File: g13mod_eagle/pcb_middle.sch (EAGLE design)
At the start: 14 parts

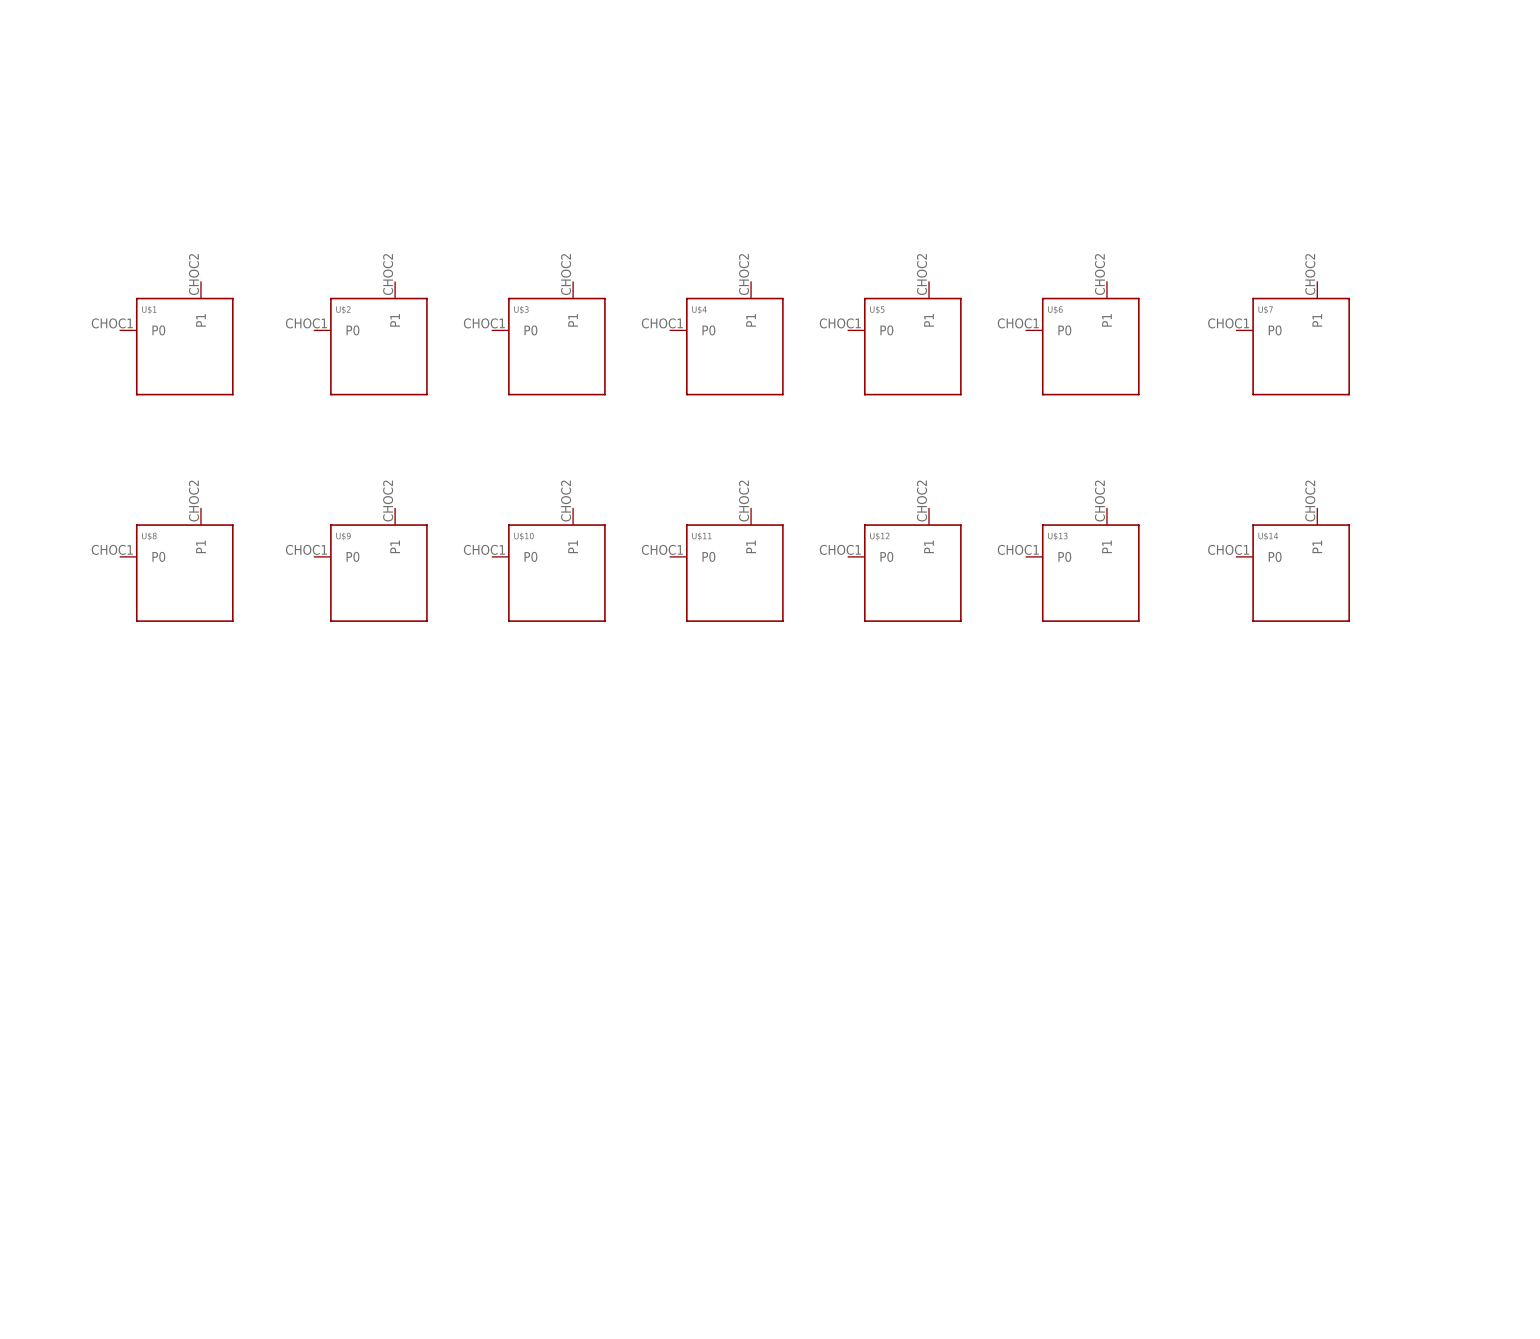
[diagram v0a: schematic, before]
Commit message: wiring middle pcb
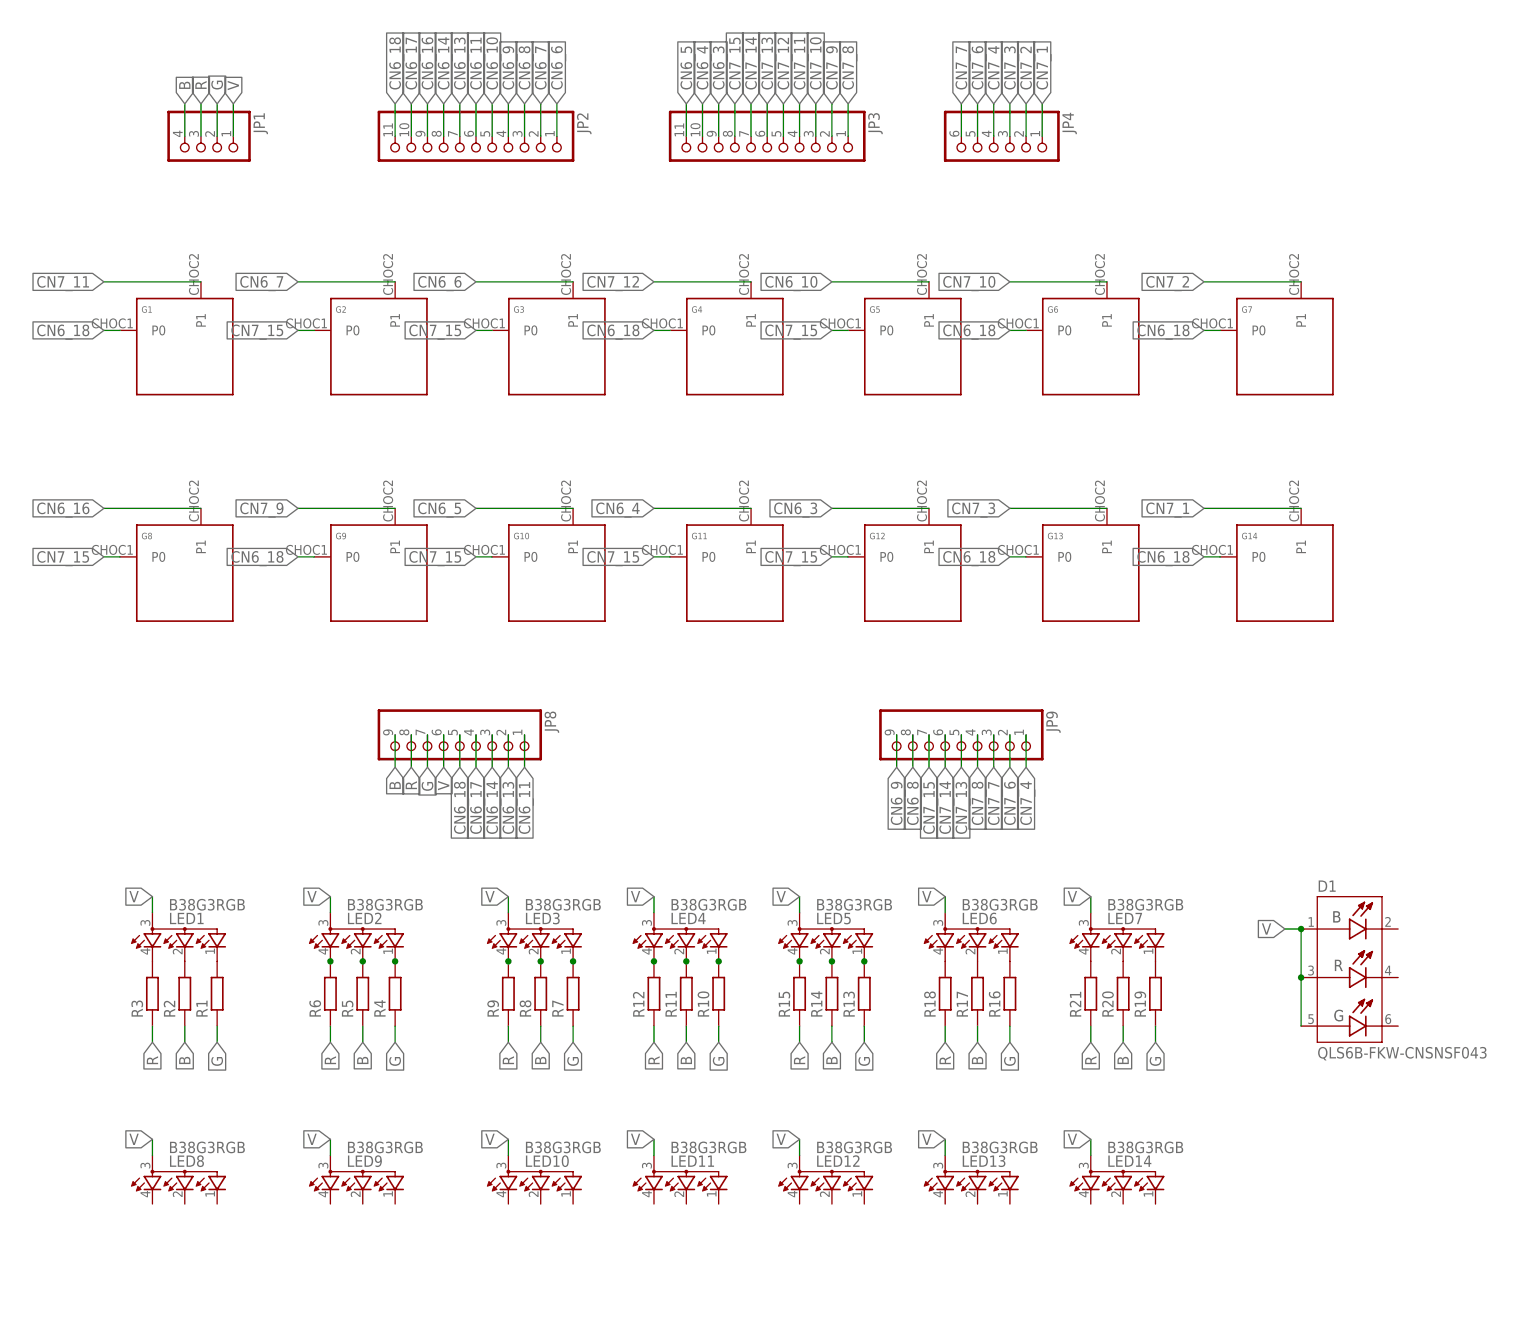
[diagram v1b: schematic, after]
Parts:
- removed U$14, U$7: KEYSWITCH-PLAIN-CHOC-1U, Keyboard:KEYSWITCH-PLAIN-CHOC-1U
- added D1: QLS6B-FKW-CNSNSF043, QLS6B-FKW-CNSNSF043:QLS6B-FKW-CNSNSF043
- added G14, G7: KEYSWITCH-PLAIN-CHOC-1U, Keyboard:KEYSWITCH-PLAIN-CHOC-1U
- added JP1: (no value), pinhead-half-pitch:THROUHOLE04
- added JP2, JP3: (no value), pinhead-half-pitch:THROUHOLE11
- added JP4: (no value), pinhead-half-pitch:THROUHOLE06
- added JP8, JP9: (no value), pinhead-half-pitch:THROUHOLE09
- added LED1, LED10, LED11, LED12, LED13, LED14, LED2, LED3, LED4, LED5, LED6, LED7, LED8, LED9: B38G3RGB, led_rgb:B38G3RGB
- added R1, R10, R11, R12, R13, R14, R15, R16, R17, R18, R19, R2, R20, R21, R3, R4, R5, R6, R7, R8, R9: (no value), rcl:R-EU_R0603
- renumbered U$1 to G1, U$10 to G10, U$11 to G11, U$12 to G12, U$13 to G13, U$2 to G2, U$3 to G3, U$4 to G4, U$5 to G5, U$6 to G6, U$8 to G8, U$9 to G9
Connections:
- new net B: JP1.4, JP8.9, R11.1, R14.1, R17.1, R2.1, R20.1, R5.1, R8.1
- new net CN6_10: G5.P1, JP2.5
- new net CN6_11: JP2.6, JP8.1
- new net CN6_13: JP2.7, JP8.2
- new net CN6_14: JP2.8, JP8.3
- new net CN6_16: G8.P1, JP2.9
- new net CN6_17: JP2.10, JP8.4
- new net CN6_18: G1.P0, G13.P0, G14.P0, G4.P0, G6.P0, G7.P0, G9.P0, JP2.11, JP8.5
- new net CN6_3: G12.P1, JP3.9
- new net CN6_4: G11.P1, JP3.10
- new net CN6_5: G10.P1, JP3.11
- new net CN6_6: G3.P1, JP2.1
- new net CN6_7: G2.P1, JP2.2
- new net CN6_8: JP2.3, JP9.8
- new net CN6_9: JP2.4, JP9.9
- new net CN7_1: G14.P1, JP4.1
- new net CN7_10: G6.P1, JP3.3
- new net CN7_11: G1.P1, JP3.4
- new net CN7_12: G4.P1, JP3.5
- new net CN7_13: JP3.6, JP9.5
- new net CN7_14: JP3.7, JP9.6
- new net CN7_15: G10.P0, G11.P0, G12.P0, G2.P0, G3.P0, G5.P0, G8.P0, JP3.8, JP9.7
- new net CN7_2: G7.P1, JP4.2
- new net CN7_3: G13.P1, JP4.3
- new net CN7_4: JP4.4, JP9.1
- new net CN7_6: JP4.5, JP9.2
- new net CN7_7: JP4.6, JP9.3
- new net CN7_8: JP3.1, JP9.4
- new net CN7_9: G9.P1, JP3.2
- new net G: JP1.2, JP8.7, R1.1, R10.1, R13.1, R16.1, R19.1, R4.1, R7.1
- new net N$1: LED1.CGREEN, R1.2
- new net N$10: LED4.CGREEN, R10.2
- new net N$11: LED4.CBLUE, R11.2
- new net N$12: LED4.CRED, R12.2
- new net N$13: LED5.CGREEN, R13.2
- new net N$14: LED5.CBLUE, R14.2
- new net N$15: LED5.CRED, R15.2
- new net N$16: LED6.CGREEN, R16.2
- new net N$17: LED6.CBLUE, R17.2
- new net N$18: LED6.CRED, R18.2
- new net N$19: LED7.CGREEN, R19.2
- new net N$2: LED1.CBLUE, R2.2
- new net N$20: LED7.CBLUE, R20.2
- new net N$21: LED7.CRED, R21.2
- new net N$3: LED1.CRED, R3.2
- new net N$4: LED2.CGREEN, R4.2
- new net N$5: LED2.CBLUE, R5.2
- new net N$6: LED2.CRED, R6.2
- new net N$7: LED3.CGREEN, R7.2
- new net N$8: LED3.CBLUE, R8.2
- new net N$9: LED3.CRED, R9.2
- new net R: JP1.3, JP8.8, R12.1, R15.1, R18.1, R21.1, R3.1, R6.1, R9.1
- new net V: D1.BLUE_ANODE, D1.GREEN_ANODE, D1.RED_ANODE, JP1.1, JP8.6, LED1.A, LED10.A, LED11.A, LED12.A, LED13.A, LED14.A, LED2.A, LED3.A, LED4.A, LED5.A, LED6.A, LED7.A, LED8.A, LED9.A

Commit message: wiring middle pcb
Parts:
- added R22, R23, R24, R25, R26, R27, R28, R29, R30: (no value), rcl:R-EU_R0603
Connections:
- new net N$22: LED8.CGREEN, R22.2
- new net N$23: LED8.CBLUE, R23.2
- new net N$24: LED8.CRED, R24.2
- new net N$25: LED9.CGREEN, R25.2
- new net N$26: LED9.CBLUE, R26.2
- new net N$27: LED9.CRED, R27.2
- new net N$28: LED10.CGREEN, R28.2
- new net N$29: LED10.CBLUE, R29.2
- new net N$30: LED10.CRED, R30.2
- net B: now also R23.1, R26.1, R29.1
- net G: now also R22.1, R25.1, R28.1
- net R: now also R24.1, R27.1, R30.1
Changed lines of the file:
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@@
 <part name="R20" library="rcl" library_urn="urn:adsk.eagle:library:334" deviceset="R-EU_" device="R0603" package3d_urn="urn:adsk.eagle:package:23555/3"/>
 <part name="R21" library="rcl" library_urn="urn:adsk.eagle:library:334" deviceset="R-EU_" device="R0603" package3d_urn="urn:adsk.eagle:package:23555/3"/>
+<part name="R22" library="rcl" library_urn="urn:adsk.eagle:library:334" deviceset="R-EU_" device="R0603" package3d_urn="urn:adsk.eagle:package:23555/3"/>
+<part name="R23" library="rcl" library_urn="urn:adsk.eagle:library:334" deviceset="R-EU_" device="R0603" package3d_urn="urn:adsk.eagle:package:23555/3"/>
+<part name="R24" library="rcl" library_urn="urn:adsk.eagle:library:334" deviceset="R-EU_" device="R0603" package3d_urn="urn:adsk.eagle:package:23555/3"/>
+<part name="R25" library="rcl" library_urn="urn:adsk.eagle:library:334" deviceset="R-EU_" device="R0603" package3d_urn="urn:adsk.eagle:package:23555/3"/>
+<part name="R26" library="rcl" library_urn="urn:adsk.eagle:library:334" deviceset="R-EU_" device="R0603" package3d_urn="urn:adsk.eagle:package:23555/3"/>
+<part name="R27" library="rcl" library_urn="urn:adsk.eagle:library:334" deviceset="R-EU_" device="R0603" package3d_urn="urn:adsk.eagle:package:23555/3"/>
+<part name="R28" library="rcl" library_urn="urn:adsk.eagle:library:334" deviceset="R-EU_" device="R0603" package3d_urn="urn:adsk.eagle:package:23555/3"/>
+<part name="R29" library="rcl" library_urn="urn:adsk.eagle:library:334" deviceset="R-EU_" device="R0603" package3d_urn="urn:adsk.eagle:package:23555/3"/>
+<part name="R30" library="rcl" library_urn="urn:adsk.eagle:library:334" deviceset="R-EU_" device="R0603" package3d_urn="urn:adsk.eagle:package:23555/3"/>
 </parts>
 <sheets>
@@
 <attribute name="VALUE" x="158.242" y="-87.63" size="1.778" layer="96" rot="R90"/>
 </instance>
+<instance part="R22" gate="G$1" x="17.78" y="-121.92" smashed="yes" rot="R90">
+<attribute name="NAME" x="16.2814" y="-125.73" size="1.778" layer="95" rot="R90"/>
+<attribute name="VALUE" x="21.082" y="-125.73" size="1.778" layer="96" rot="R90"/>
+</instance>
+<instance part="R23" gate="G$1" x="12.7" y="-121.92" smashed="yes" rot="R90">
+<attribute name="NAME" x="11.2014" y="-125.73" size="1.778" layer="95" rot="R90"/>
+<attribute name="VALUE" x="16.002" y="-125.73" size="1.778" layer="96" rot="R90"/>
+</instance>
+<instance part="R24" gate="G$1" x="7.62" y="-121.92" smashed="yes" rot="R90">
+<attribute name="NAME" x="6.1214" y="-125.73" size="1.778" layer="95" rot="R90"/>
+<attribute name="VALUE" x="10.922" y="-125.73" size="1.778" layer="96" rot="R90"/>
+</instance>
+<instance part="R25" gate="G$1" x="45.72" y="-121.92" smashed="yes" rot="R90">
+<attribute name="NAME" x="44.2214" y="-125.73" size="1.778" layer="95" rot="R90"/>
+<attribute name="VALUE" x="49.022" y="-125.73" size="1.778" layer="96" rot="R90"/>
+</instance>
+<instance part="R26" gate="G$1" x="40.64" y="-121.92" smashed="yes" rot="R90">
+<attribute name="NAME" x="39.1414" y="-125.73" size="1.778" layer="95" rot="R90"/>
+<attribute name="VALUE" x="43.942" y="-125.73" size="1.778" layer="96" rot="R90"/>
+</instance>
+<instance part="R27" gate="G$1" x="35.56" y="-121.92" smashed="yes" rot="R90">
+<attribute name="NAME" x="34.0614" y="-125.73" size="1.778" layer="95" rot="R90"/>
+<attribute name="VALUE" x="38.862" y="-125.73" size="1.778" layer="96" rot="R90"/>
+</instance>
+<instance part="R28" gate="G$1" x="73.66" y="-121.92" smashed="yes" rot="R90">
+<attribute name="NAME" x="72.1614" y="-125.73" size="1.778" layer="95" rot="R90"/>
+<attribute name="VALUE" x="76.962" y="-125.73" size="1.778" layer="96" rot="R90"/>
+</instance>
+<instance part="R29" gate="G$1" x="68.58" y="-121.92" smashed="yes" rot="R90">
+<attribute name="NAME" x="67.0814" y="-125.73" size="1.778" layer="95" rot="R90"/>
+<attribute name="VALUE" x="71.882" y="-125.73" size="1.778" layer="96" rot="R90"/>
+</instance>
+<instance part="R30" gate="G$1" x="63.5" y="-121.92" smashed="yes" rot="R90">
+<attribute name="NAME" x="62.0014" y="-125.73" size="1.778" layer="95" rot="R90"/>
+<attribute name="VALUE" x="66.802" y="-125.73" size="1.778" layer="96" rot="R90"/>
+</instance>
 </instances>
 <busses>
@@
 <label x="160.02" y="-91.44" size="1.778" layer="95" rot="R270" xref="yes"/>
 </segment>
+<segment>
+<pinref part="R23" gate="G$1" pin="1"/>
+<wire x1="12.7" y1="-127" x2="12.7" y2="-129.54" width="0.1524" layer="91"/>
+<label x="12.7" y="-129.54" size="1.778" layer="95" rot="R270" xref="yes"/>
+</segment>
+<segment>
+<pinref part="R26" gate="G$1" pin="1"/>
+<wire x1="40.64" y1="-127" x2="40.64" y2="-129.54" width="0.1524" layer="91"/>
+<label x="40.64" y="-129.54" size="1.778" layer="95" rot="R270" xref="yes"/>
+</segment>
+<segment>
+<pinref part="R29" gate="G$1" pin="1"/>
+<wire x1="68.58" y1="-127" x2="68.58" y2="-129.54" width="0.1524" layer="91"/>
+<label x="68.58" y="-129.54" size="1.778" layer="95" rot="R270" xref="yes"/>
+</segment>
 </net>
 <net name="R" class="0">
@@
 <label x="154.94" y="-91.44" size="1.778" layer="95" rot="R270" xref="yes"/>
 </segment>
+<segment>
+<pinref part="R24" gate="G$1" pin="1"/>
+<wire x1="7.62" y1="-127" x2="7.62" y2="-129.54" width="0.1524" layer="91"/>
+<label x="7.62" y="-129.54" size="1.778" layer="95" rot="R270" xref="yes"/>
+</segment>
+<segment>
+<pinref part="R27" gate="G$1" pin="1"/>
+<wire x1="35.56" y1="-127" x2="35.56" y2="-129.54" width="0.1524" layer="91"/>
+<label x="35.56" y="-129.54" size="1.778" layer="95" rot="R270" xref="yes"/>
+</segment>
+<segment>
+<pinref part="R30" gate="G$1" pin="1"/>
+<wire x1="63.5" y1="-127" x2="63.5" y2="-129.54" width="0.1524" layer="91"/>
+<label x="63.5" y="-129.54" size="1.778" layer="95" rot="R270" xref="yes"/>
+</segment>
 </net>
 <net name="G" class="0">
@@
 <wire x1="165.1" y1="-88.9" x2="165.1" y2="-91.44" width="0.1524" layer="91"/>
 <label x="165.1" y="-91.44" size="1.778" layer="95" rot="R270" xref="yes"/>
+</segment>
+<segment>
+<pinref part="R22" gate="G$1" pin="1"/>
+<wire x1="17.78" y1="-127" x2="17.78" y2="-129.54" width="0.1524" layer="91"/>
+<label x="17.78" y="-129.54" size="1.778" layer="95" rot="R270" xref="yes"/>
+</segment>
+<segment>
+<pinref part="R25" gate="G$1" pin="1"/>
+<wire x1="45.72" y1="-127" x2="45.72" y2="-129.54" width="0.1524" layer="91"/>
+<label x="45.72" y="-129.54" size="1.778" layer="95" rot="R270" xref="yes"/>
+</segment>
+<segment>
+<pinref part="R28" gate="G$1" pin="1"/>
+<wire x1="73.66" y1="-127" x2="73.66" y2="-129.54" width="0.1524" layer="91"/>
+<label x="73.66" y="-129.54" size="1.778" layer="95" rot="R270" xref="yes"/>
 </segment>
 </net>
@@
 </segment>
 </net>
+<net name="N$22" class="0">
+<segment>
+<pinref part="R22" gate="G$1" pin="2"/>
+<pinref part="LED8" gate="G$1" pin="CGREEN"/>
+</segment>
+</net>
+<net name="N$23" class="0">
+<segment>
+<pinref part="R23" gate="G$1" pin="2"/>
+<pinref part="LED8" gate="G$1" pin="CBLUE"/>
+</segment>
+</net>
+<net name="N$24" class="0">
+<segment>
+<pinref part="R24" gate="G$1" pin="2"/>
+<pinref part="LED8" gate="G$1" pin="CRED"/>
+</segment>
+</net>
+<net name="N$25" class="0">
+<segment>
+<pinref part="R25" gate="G$1" pin="2"/>
+<pinref part="LED9" gate="G$1" pin="CGREEN"/>
+</segment>
+</net>
+<net name="N$26" class="0">
+<segment>
+<pinref part="R26" gate="G$1" pin="2"/>
+<pinref part="LED9" gate="G$1" pin="CBLUE"/>
+</segment>
+</net>
+<net name="N$27" class="0">
+<segment>
+<pinref part="R27" gate="G$1" pin="2"/>
+<pinref part="LED9" gate="G$1" pin="CRED"/>
+</segment>
+</net>
+<net name="N$28" class="0">
+<segment>
+<pinref part="R28" gate="G$1" pin="2"/>
+<pinref part="LED10" gate="G$1" pin="CGREEN"/>
+</segment>
+</net>
+<net name="N$29" class="0">
+<segment>
+<pinref part="R29" gate="G$1" pin="2"/>
+<pinref part="LED10" gate="G$1" pin="CBLUE"/>
+</segment>
+</net>
+<net name="N$30" class="0">
+<segment>
+<pinref part="R30" gate="G$1" pin="2"/>
+<pinref part="LED10" gate="G$1" pin="CRED"/>
+</segment>
+</net>
